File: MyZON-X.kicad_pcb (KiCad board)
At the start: 2 copper layers, 63.5 x 101 mm, 29 parts, among them SW1 SW_DIP_x03, U1 AY-3-8910, U2 74HCT74, U3 74HCT08, U4 74HCT11, U5 74HCT02

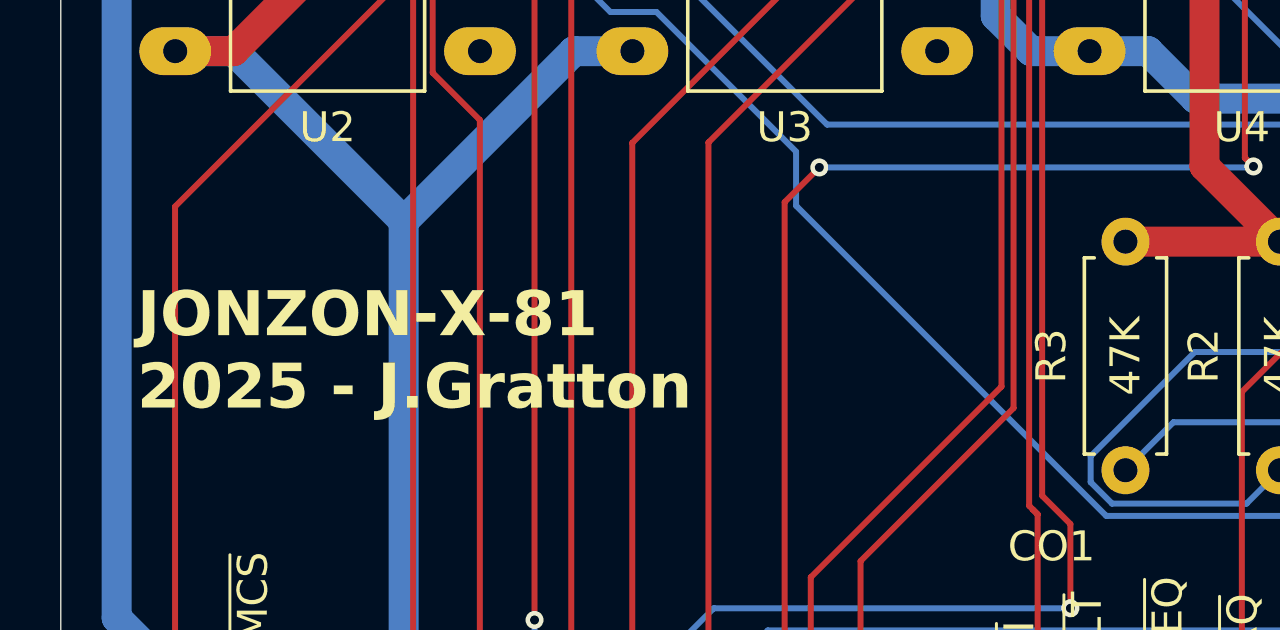
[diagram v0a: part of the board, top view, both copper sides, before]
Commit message: Added Fab Files Added Revision to PCB
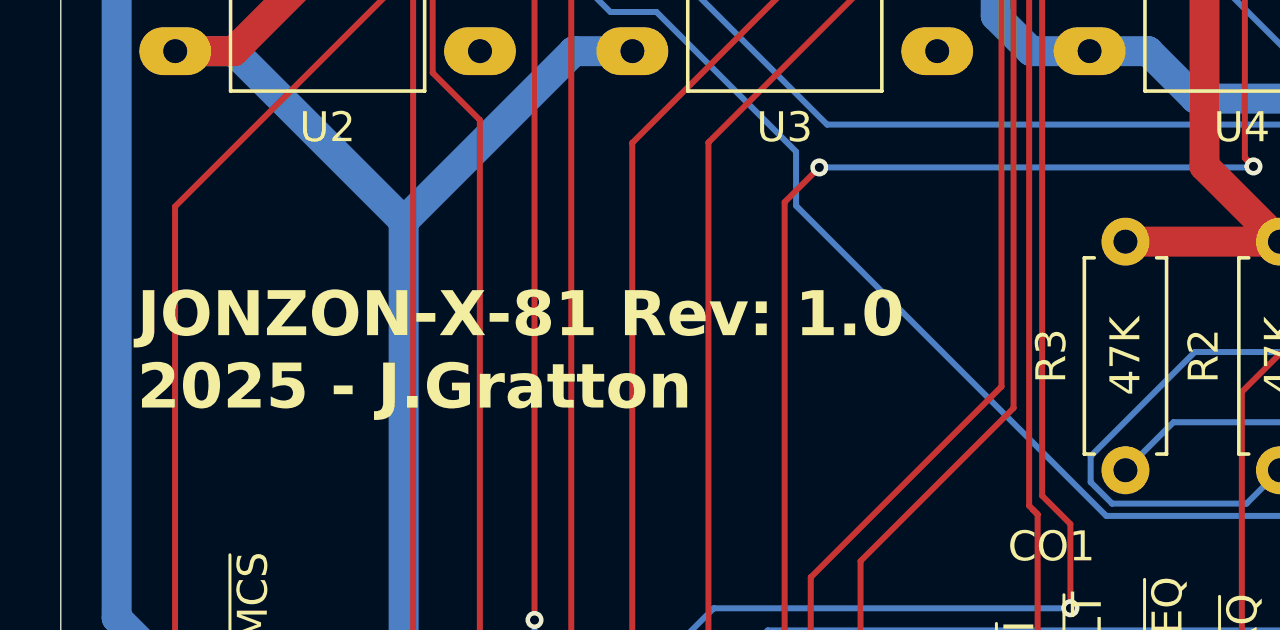
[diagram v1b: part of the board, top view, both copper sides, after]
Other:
- board text added: "JONZON-X-81 Rev: 1.0 2025 - J.Gratton"
- board text removed: "JONZON-X-81 2025 - J.Gratton"
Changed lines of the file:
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@@
 	)
 	(paper "A4")
+	(title_block
+		(title "JONZON-X-81")
+		(date "2025-08-11")
+		(rev "1.0")
+	)
 	(layers
 		(0 "F.Cu" signal)
@@
 			(drillshape 0)
 			(scaleselection 1)
-			(outputdirectory "")
+			(outputdirectory "FabFiles")
 		)
 	)
@@
 		(layer "Edge.Cuts")
 	)
-	(gr_text "JONZON-X-81\n2025 - J.Gratton"
+	(gr_text "JONZON-X-81 Rev: 1.0\n2025 - J.Gratton"
 		(at 54.61 131.445 0)
 		(layer "F.SilkS")

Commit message: Changed Label on LINEIN to THROUGH Added seperate Ground and Audio Ground Added 0ohm link for Ground to Audio Ground link Could be a Ferrite Bead
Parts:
- added R12: 0R, Resistor_THT:R_Axial_DIN0207_L6.3mm_D2.5mm_P7.62mm_Horizontal, F.Cu at (57.1, 59.1)
- CO3: value LINEIN -> THROUGH
- moved R5 4.45 mm to (97.2, 71.1)
- moved R6 4.45 mm to (92.1, 63.5)
- moved R7 4.45 mm to (87.0, 63.5)
- moved R8 4.45 mm to (81.9, 63.5)
- moved C3 4.45 mm to (59.1, 63.5)
- moved C4 4.45 mm to (59.1, 71.1)
- moved R11 4.45 mm to (66.7, 71.1)
- moved R10 4.44 mm to (71.8, 63.5)
- moved R4 4.44 mm to (102.2, 71.1)
- moved R9 4.44 mm to (76.8, 63.5)
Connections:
- C3 pad 2: GND -> GND_AUDIO
- C4 pad 2: GND -> GND_AUDIO
- CO2 pad 5: GND -> GND_AUDIO
- CO3 pad 3: GND -> GND_AUDIO
- R8 pad 2: GND -> GND_AUDIO
- R9 pad 2: GND -> GND_AUDIO
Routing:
- net GND_AUDIO: track 0.00 -> 97.4 mm
- net GND: track 289.8 -> 229.9 mm
- net Net-(CO3-Pin_2): track 85.2 -> 66.5 mm, vias 0 -> 1
- net /VALID: track 29.3 -> 45.1 mm, vias 0 -> 2
- net Net-(R2-Pad2): track 51.6 -> 38.9 mm, vias 1 -> 0
- net Net-(U3-Pad6): track 47.4 -> 35.1 mm
- net /A7: track 55.1 -> 65.9 mm, vias 0 -> 1
- net /D7: track 73.7 -> 83.5 mm
- net VCC: track 239.2 -> 230.1 mm
- net Net-(R1-Pad2): track 38.1 -> 30.9 mm
- net /~{RESET}: track 102.0 -> 95.4 mm, vias 1 -> 2
- net /D3: track 71.4 -> 65.0 mm, vias 2 -> 0
- net /~{IOREQ}: track 62.2 -> 67.2 mm, vias 1 -> 0
- net Net-(CO3-Pin_1): track 63.9 -> 68.9 mm, vias 0 -> 1
- net Net-(C1-Pad1): track 36.4 -> 41.3 mm
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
